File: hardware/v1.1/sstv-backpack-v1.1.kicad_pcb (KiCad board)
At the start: 2 copper layers, 38.1 x 63.5 mm, 27 parts, among them J1 Conn_01x03_Pin, J2 Conn_01x02_Pin, J4 USB_C_Receptacle_USB2.0_14P, Q2 2N3904, SW1 SW_Push, SW2 SLW-1276864-4A-D, U1 ESP32-CAM, U2 FT231XS

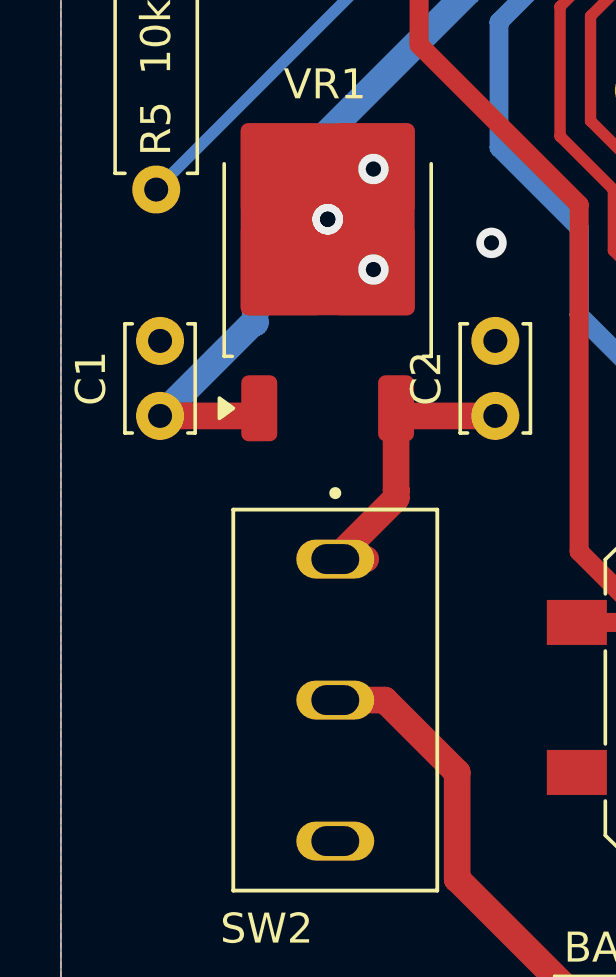
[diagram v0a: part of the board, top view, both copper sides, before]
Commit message: Update README and add pull-down resistors for PTT
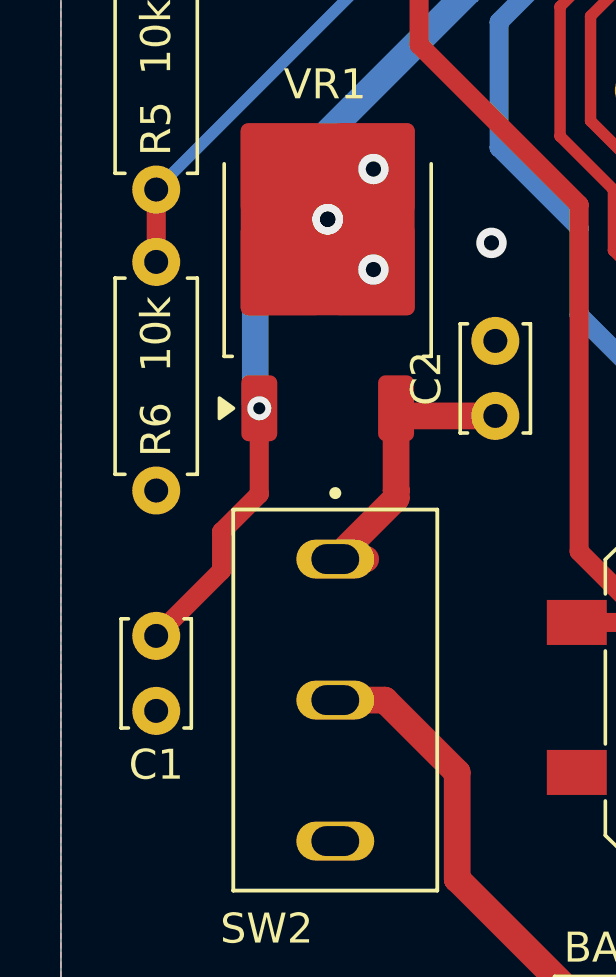
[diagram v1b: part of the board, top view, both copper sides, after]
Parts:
- added R6: 10k, Resistor_THT:R_Axial_DIN0207_L6.3mm_D2.5mm_P7.62mm_Horizontal, F.Cu at (142.9, 106.9)
- moved C1 7.33 mm to (142.9, 111.8), turned to -90 degrees
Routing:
- net /5VO: track 47.2 -> 51.3 mm, vias 0 -> 1
- net PTT_TRIG: track 21.6 -> 24.0 mm
